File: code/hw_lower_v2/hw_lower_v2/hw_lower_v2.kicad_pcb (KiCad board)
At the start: 2 copper layers, 112 parts, among them J1 Screw_Terminal_01x01, J10 Conn_01x02, J11 Conn_01x02, J12 Conn_01x02, J13 Conn_01x02, J14 Conn_01x02, J2 Screw_Terminal_01x01, J3 Screw_Terminal_01x01, J4 Screw_Terminal_01x01, J5 Screw_Terminal_01x01, J6 Screw_Terminal_01x01, J7 Conn_01x06_Pin, J8 Conn_02x20_Odd_Even, J9 Conn_01x02, K1 AHES4191, Q1 BSS138, Q2 BSS138, Q3 BSS138, T1 TS3193-2C 2mA/2mA, U1 BRCS02C, U2 BL0942, U3 DRV8220DRL, U4 TLV1805, U5 ICL7660A, U6 AMS1117, U7 AMS1117

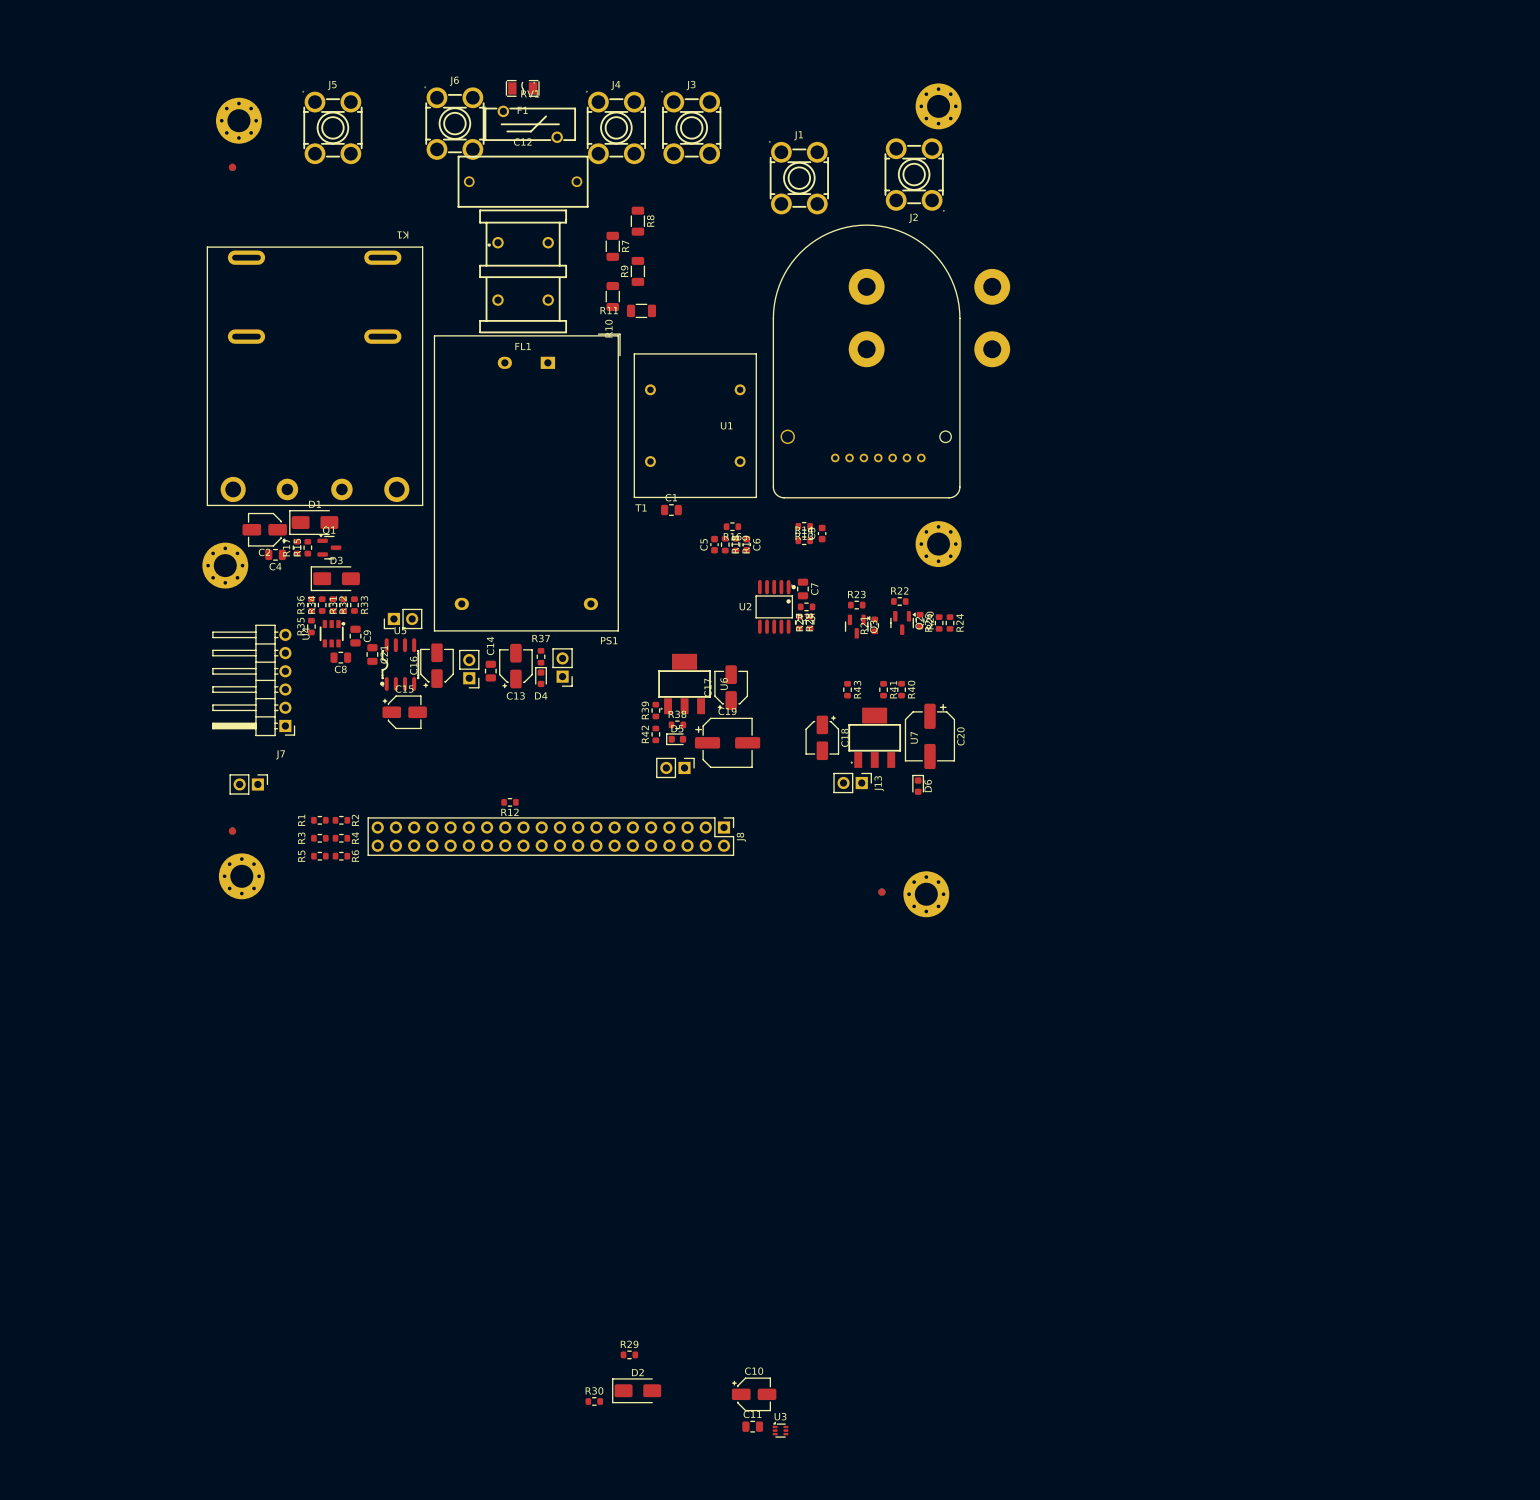
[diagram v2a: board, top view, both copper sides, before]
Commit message: Preliminary pcb component placement done
PCB size currently is around 100mm X 100mm with the mezanine board being ~40mm x 100mm
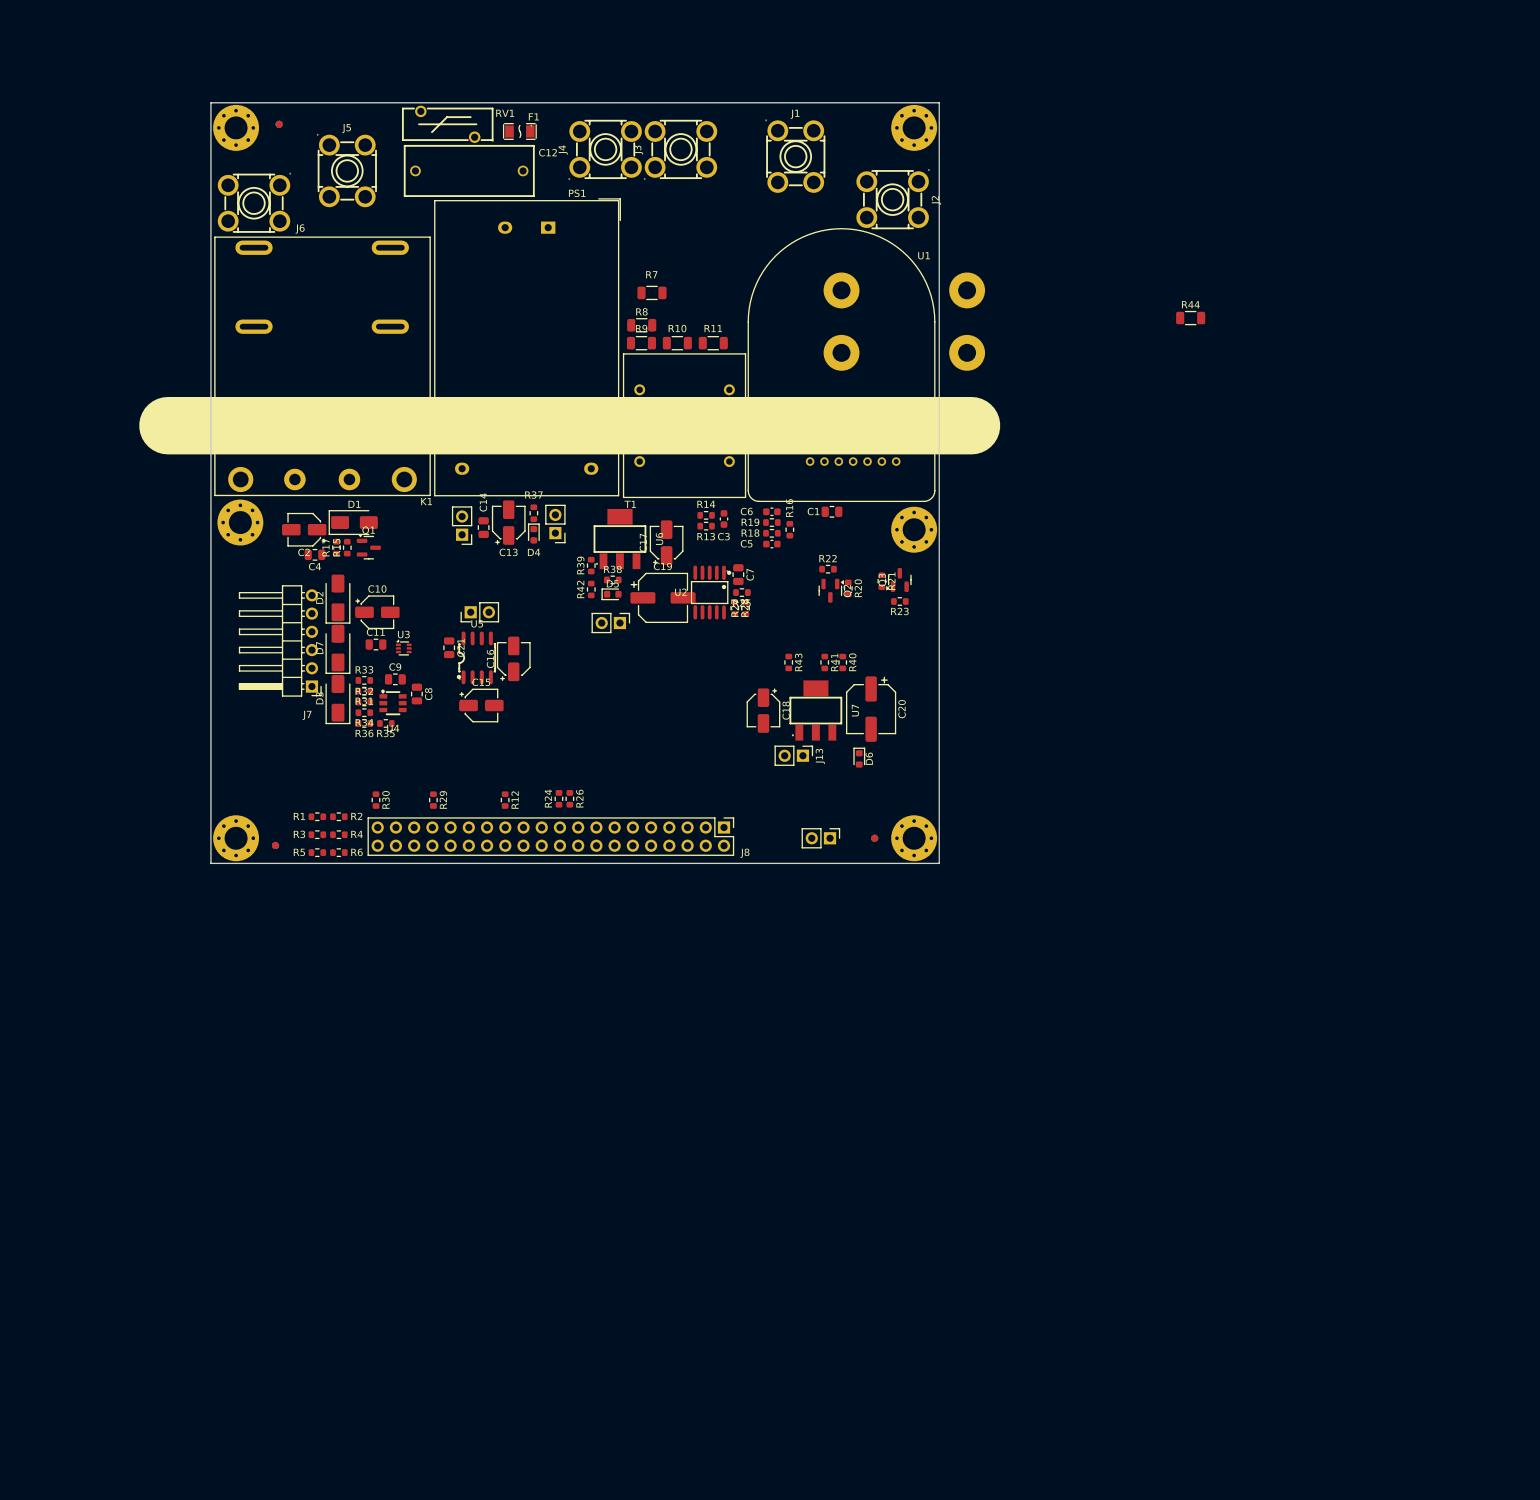
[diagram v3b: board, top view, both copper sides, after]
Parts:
- removed FL1: Filter_EMI_CommonMode, JLCPCB:FILTER-TH_4P-L17.0-W12.0-P7.00-D0.6-S8.00
- added D7: SMAJ5.0A, Diode_SMD:D_SMA, F.Cu at (59.7, 105.0)
- added R44: 1M, Resistor_SMD:R_1206_3216Metric, F.Cu at (178.5, 59.0)
- moved C10 121.0 mm to (65.2, 100.0)
- moved C11 121.0 mm to (65.0, 104.5)
- moved U3 121.0 mm to (68.9, 105.0)
- moved D2 118.1 mm to (59.7, 98.0), turned to 90 degrees
- moved R30 89.2 mm to (65.0, 126.2), turned to -90 degrees
- moved R29 82.0 mm to (73.0, 126.2), turned to -90 degrees
- moved J14 80.1 mm to (128.3, 131.5)
- moved R24 59.8 mm to (90.5, 126.0), turned to 90 degrees
- moved R26 57.0 mm to (92.0, 126.0), turned to -90 degrees
- moved J6 30.1 mm to (48.0, 43.0), turned to -90 degrees
- moved C1 22.4 mm to (128.6, 86.0)
- moved C17 22.1 mm to (105.5, 90.3)
- moved C19 22.1 mm to (105.0, 98.0)
- moved D5 22.1 mm to (98.0, 97.5)
- moved J12 22.1 mm to (99.0, 101.5)
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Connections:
- C1 pad 2: Earth_Protective -> GND
- C12 pad 1: Net-(C12-Pad1) -> Net-(PS1-AC/L)
- C2 pad 2: Earth_Protective -> GND
- C3 pad 2: Earth_Protective -> GND
- C4 pad 2: Earth_Protective -> GND
- C5 pad 2: Earth_Protective -> GND
- C6 pad 1: Earth_Protective -> GND
- C7 pad 2: Earth_Protective -> GND
- F1 pad 2: Net-(C12-Pad1) -> Net-(PS1-AC/L)
- K1 pad 3: Earth_Protective -> GND
- PS1 pad 2: Net-(PS1-AC/N) -> /AC/N_in
- Q1 pad 2: Earth_Protective -> GND
- R13 pad 1: Earth_Protective -> GND
- R15 pad 1: Earth_Protective -> GND
- R26 pad 1: Earth_Protective -> GND
- R28 pad 2: Earth_Protective -> GND
- RV1 pad 1: Net-(C12-Pad1) -> Net-(PS1-AC/L)
- T1 pad 3: Earth_Protective -> GND
- U1 pad 4: Earth_Protective -> GND
- U2 pad 5: Earth_Protective -> GND
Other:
- board outline added: 101.5 x 106 mm
- copper layers 2 -> 4
- board text added: "1"

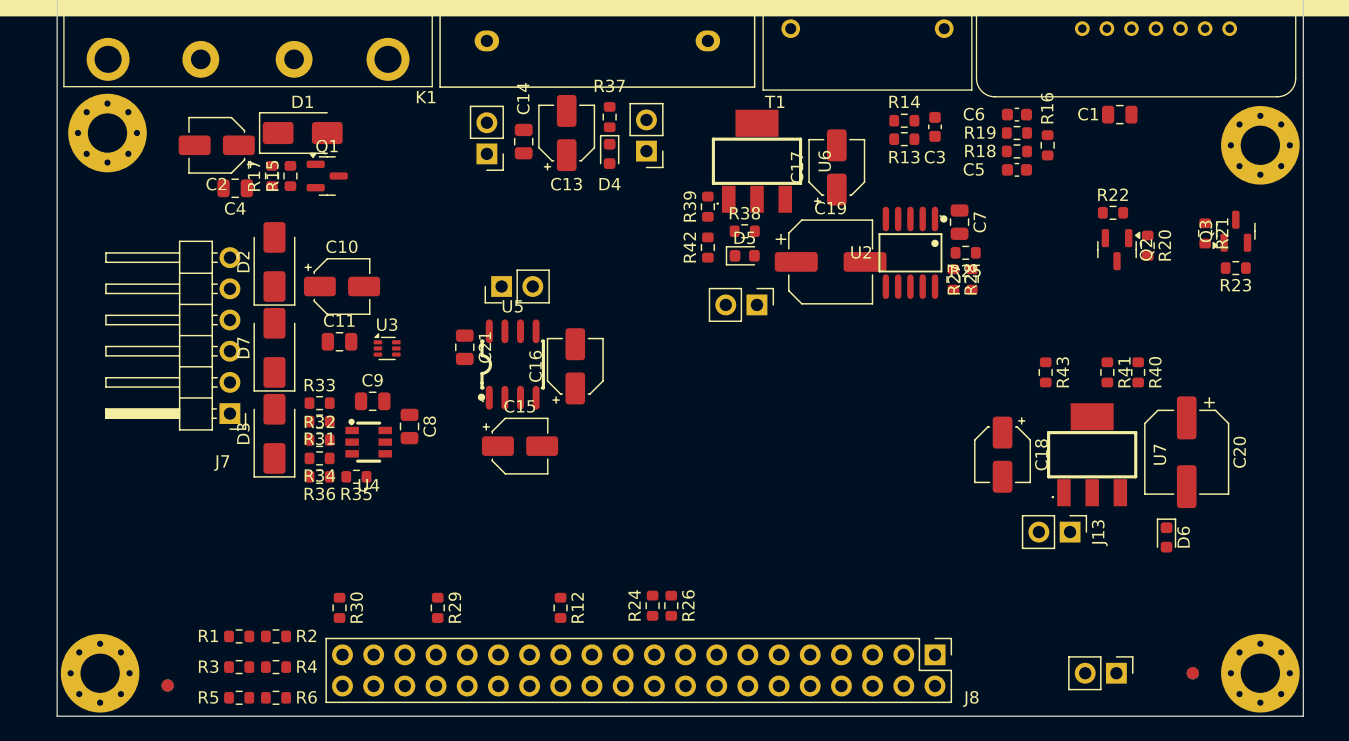
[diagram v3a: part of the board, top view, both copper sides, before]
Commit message: grouped and positioned components
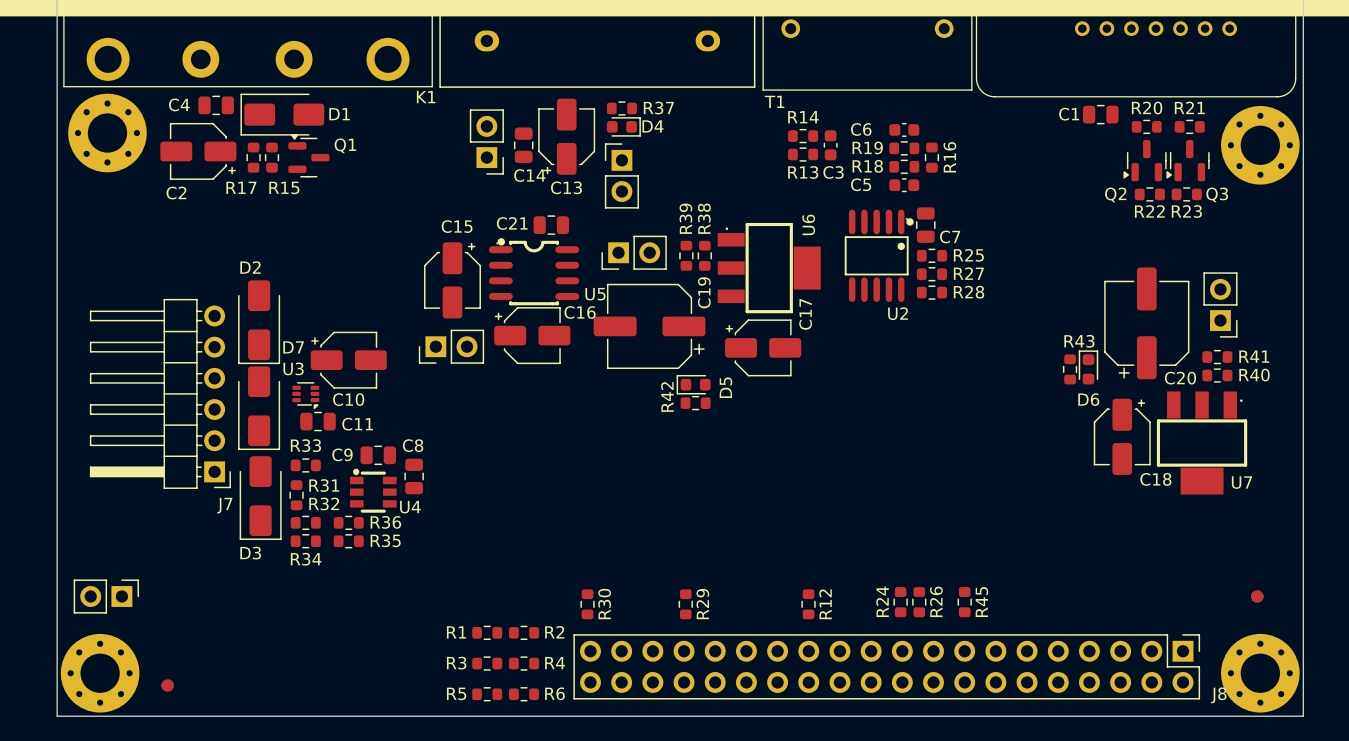
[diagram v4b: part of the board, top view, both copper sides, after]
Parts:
- added R45: 10K, Resistor_SMD:R_0603_1608Metric, F.Cu at (115.9, 125.7)
- moved J14 81.2 mm to (47.3, 125.2)
- moved J13 21.1 mm to (136.8, 102.8), turned to 180 degrees
- moved R1 20.2 mm to (77.0, 128.2)
- moved R12 20.2 mm to (103.2, 125.9)
- moved R2 20.2 mm to (80.0, 128.2)
- moved R24 20.2 mm to (110.7, 125.7)
- moved R26 20.2 mm to (112.2, 125.7)
- moved R29 20.2 mm to (93.2, 125.9)
- moved R3 20.2 mm to (77.0, 130.7)
- moved R30 20.2 mm to (85.2, 125.9)
- moved R4 20.2 mm to (80.0, 130.7)
- moved R5 20.2 mm to (77.0, 133.2)
- moved R6 20.2 mm to (80.0, 133.2)
- moved J8 20.2 mm to (133.7, 129.7)
- moved C17 15.9 mm to (99.5, 105.0), turned to 0 degrees
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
